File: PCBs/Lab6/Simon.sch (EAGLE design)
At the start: 17 parts

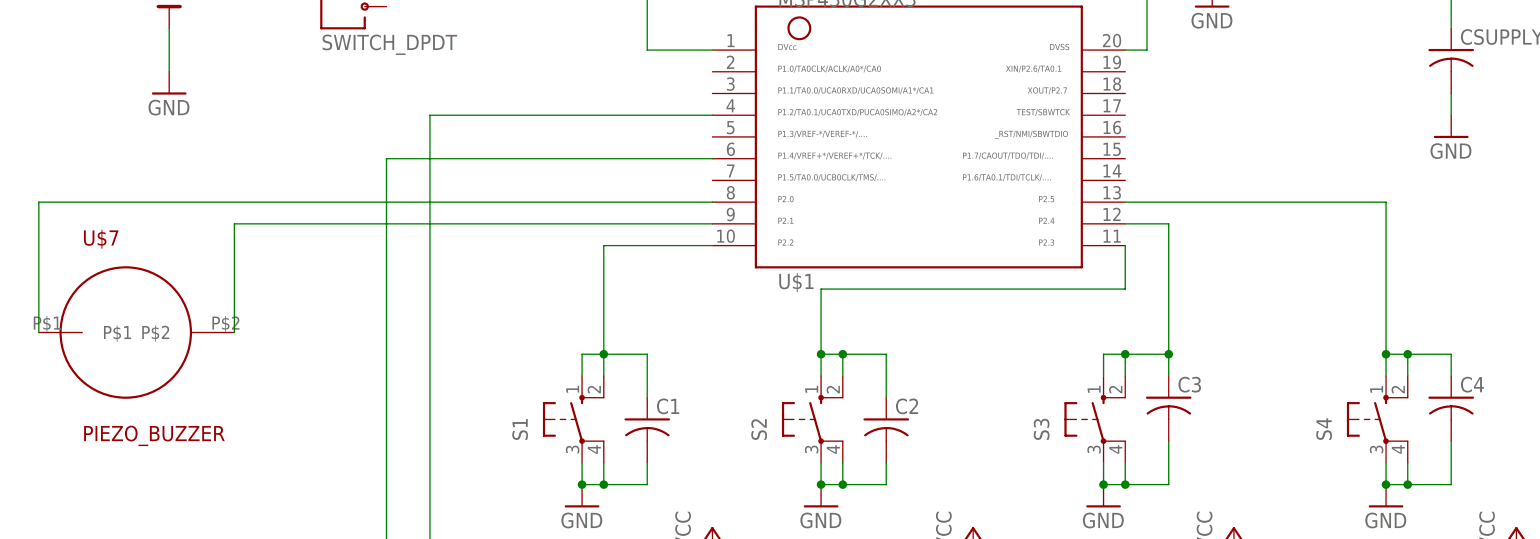
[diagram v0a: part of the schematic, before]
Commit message: Fixed buzzer connections
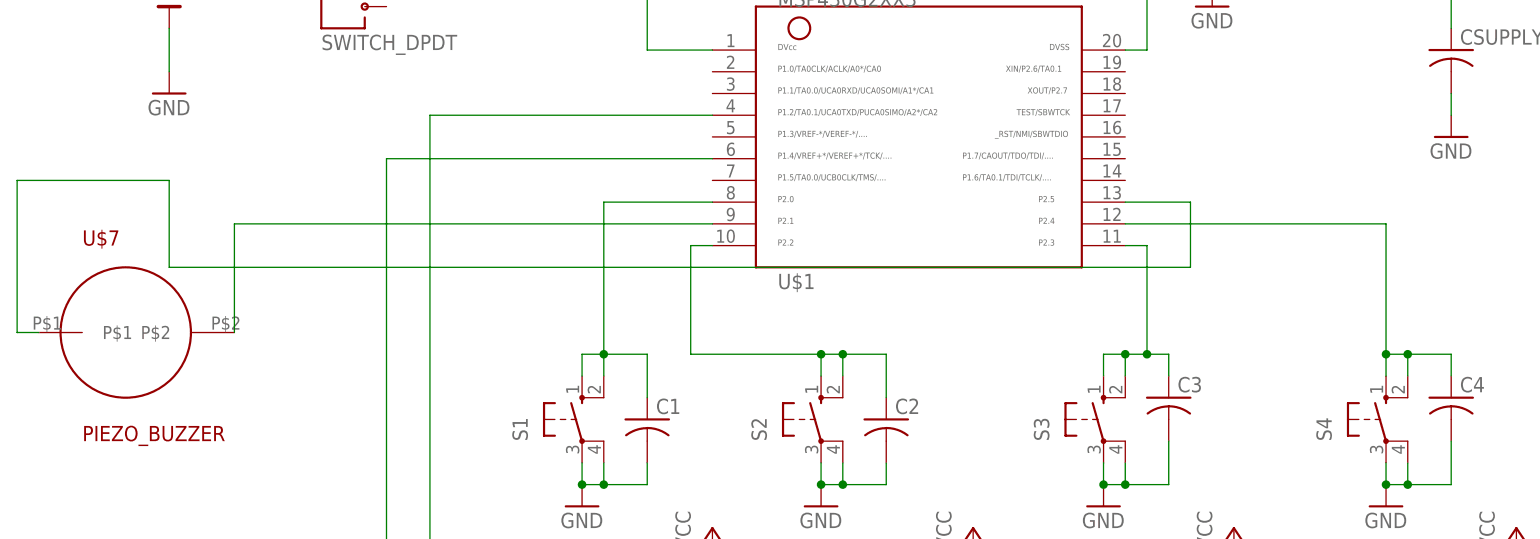
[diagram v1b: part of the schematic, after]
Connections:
- net N$11: now also U$1.13; no longer U$1.8
- net N$13: now also U$1.8; no longer U$1.10
- net N$14: now also U$1.10; no longer U$1.11
- net N$15: now also U$1.11; no longer U$1.12
- net N$16: now also U$1.12; no longer U$1.13
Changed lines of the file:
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@@
 <setting verticaltext="up"/>
 </settings>
-<grid distance="0.1" unitdist="inch" unit="inch" style="lines" multiple="1" display="yes" altdistance="0.01" altunitdist="inch" altunit="inch"/>
+<grid distance="0.1" unitdist="inch" unit="inch" style="lines" multiple="1" display="no" altdistance="0.01" altunitdist="inch" altunit="inch"/>
 <layers>
 <layer number="1" name="Top" color="4" fill="1" visible="no" active="no"/>
@@
 <wire x1="2.54" y1="-22.86" x2="2.54" y2="-27.94" width="0.1524" layer="91"/>
 <junction x="-2.54" y="-22.86"/>
-<pinref part="U$1" gate="G$1" pin="10"/>
-<wire x1="10.16" y1="-10.16" x2="-2.54" y2="-10.16" width="0.1524" layer="91"/>
-<wire x1="-2.54" y1="-10.16" x2="-2.54" y2="-22.86" width="0.1524" layer="91"/>
+<wire x1="-2.54" y1="-5.08" x2="-2.54" y2="-22.86" width="0.1524" layer="91"/>
+<pinref part="U$1" gate="G$1" pin="8"/>
+<wire x1="-2.54" y1="-5.08" x2="10.16" y2="-5.08" width="0.1524" layer="91"/>
 </segment>
 </net>
@@
 <wire x1="30.48" y1="-22.86" x2="30.48" y2="-27.94" width="0.1524" layer="91"/>
 <junction x="25.4" y="-22.86"/>
-<pinref part="U$1" gate="G$1" pin="11"/>
-<wire x1="58.42" y1="-10.16" x2="58.42" y2="-15.24" width="0.1524" layer="91"/>
-<wire x1="58.42" y1="-15.24" x2="22.86" y2="-15.24" width="0.1524" layer="91"/>
-<wire x1="22.86" y1="-15.24" x2="22.86" y2="-22.86" width="0.1524" layer="91"/>
+<pinref part="U$1" gate="G$1" pin="10"/>
+<wire x1="10.16" y1="-10.16" x2="7.62" y2="-10.16" width="0.1524" layer="91"/>
+<wire x1="7.62" y1="-10.16" x2="7.62" y2="-22.86" width="0.1524" layer="91"/>
+<wire x1="7.62" y1="-22.86" x2="22.86" y2="-22.86" width="0.1524" layer="91"/>
 </segment>
 </net>
@@
 <pinref part="C3" gate="G$1" pin="1"/>
 <wire x1="63.5" y1="-25.4" x2="63.5" y2="-22.86" width="0.1524" layer="91"/>
-<wire x1="63.5" y1="-22.86" x2="58.42" y2="-22.86" width="0.1524" layer="91"/>
+<wire x1="63.5" y1="-22.86" x2="60.96" y2="-22.86" width="0.1524" layer="91"/>
 <junction x="58.42" y="-22.86"/>
-<pinref part="U$1" gate="G$1" pin="12"/>
-<wire x1="58.42" y1="-7.62" x2="63.5" y2="-7.62" width="0.1524" layer="91"/>
-<wire x1="63.5" y1="-7.62" x2="63.5" y2="-22.86" width="0.1524" layer="91"/>
-<junction x="63.5" y="-22.86"/>
+<pinref part="U$1" gate="G$1" pin="11"/>
+<wire x1="60.96" y1="-22.86" x2="58.42" y2="-22.86" width="0.1524" layer="91"/>
+<wire x1="58.42" y1="-10.16" x2="60.96" y2="-10.16" width="0.1524" layer="91"/>
+<wire x1="60.96" y1="-10.16" x2="60.96" y2="-22.86" width="0.1524" layer="91"/>
+<junction x="60.96" y="-22.86"/>
 </segment>
 </net>
@@
 <segment>
 <pinref part="S4" gate="1" pin="S"/>
-<wire x1="88.9" y1="-5.08" x2="88.9" y2="-22.86" width="0.1524" layer="91"/>
 <pinref part="S4" gate="1" pin="S1"/>
+<wire x1="88.9" y1="-7.62" x2="88.9" y2="-22.86" width="0.1524" layer="91"/>
 <wire x1="88.9" y1="-22.86" x2="88.9" y2="-25.4" width="0.1524" layer="91"/>
 <wire x1="91.44" y1="-25.4" x2="91.44" y2="-22.86" width="0.1524" layer="91"/>
@@
 <wire x1="96.52" y1="-22.86" x2="96.52" y2="-25.4" width="0.1524" layer="91"/>
 <junction x="91.44" y="-22.86"/>
-<pinref part="U$1" gate="G$1" pin="13"/>
-<wire x1="58.42" y1="-5.08" x2="88.9" y2="-5.08" width="0.1524" layer="91"/>
+<pinref part="U$1" gate="G$1" pin="12"/>
+<wire x1="58.42" y1="-7.62" x2="88.9" y2="-7.62" width="0.1524" layer="91"/>
 </segment>
 </net>
@@
 <net name="N$11" class="0">
 <segment>
-<pinref part="U$1" gate="G$1" pin="8"/>
+<pinref part="U$1" gate="G$1" pin="13"/>
+<wire x1="58.42" y1="-5.08" x2="66.04" y2="-5.08" width="0.1524" layer="91"/>
+<wire x1="66.04" y1="-5.08" x2="66.04" y2="-12.7" width="0.1524" layer="91"/>
+<wire x1="66.04" y1="-12.7" x2="-53.34" y2="-12.7" width="0.1524" layer="91"/>
+<wire x1="-53.34" y1="-12.7" x2="-53.34" y2="-2.54" width="0.1524" layer="91"/>
+<wire x1="-53.34" y1="-2.54" x2="-71.12" y2="-2.54" width="0.1524" layer="91"/>
+<wire x1="-71.12" y1="-2.54" x2="-71.12" y2="-20.32" width="0.1524" layer="91"/>
 <pinref part="U$7" gate="G$1" pin="P$1"/>
-<wire x1="10.16" y1="-5.08" x2="-68.58" y2="-5.08" width="0.1524" layer="91"/>
-<wire x1="-68.58" y1="-5.08" x2="-68.58" y2="-20.32" width="0.1524" layer="91"/>
-</segment>
-</net>
+<wire x1="-71.12" y1="-20.32" x2="-68.58" y2="-20.32" width="0.1524" layer="91"/>
+</segment>
+</net>

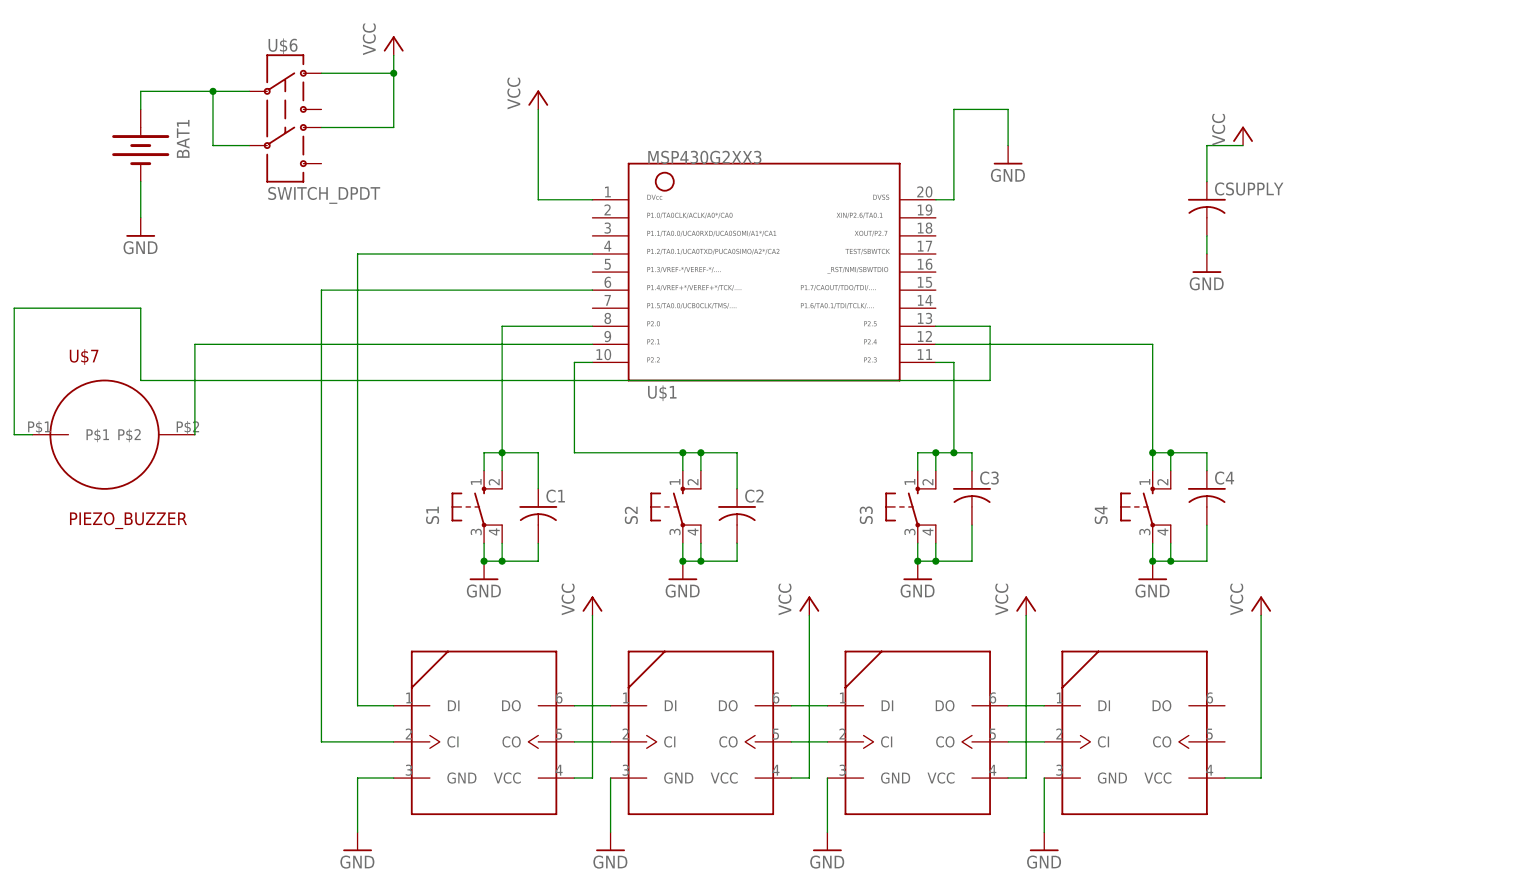
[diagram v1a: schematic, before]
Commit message: Switched to Xin Huang's schematic
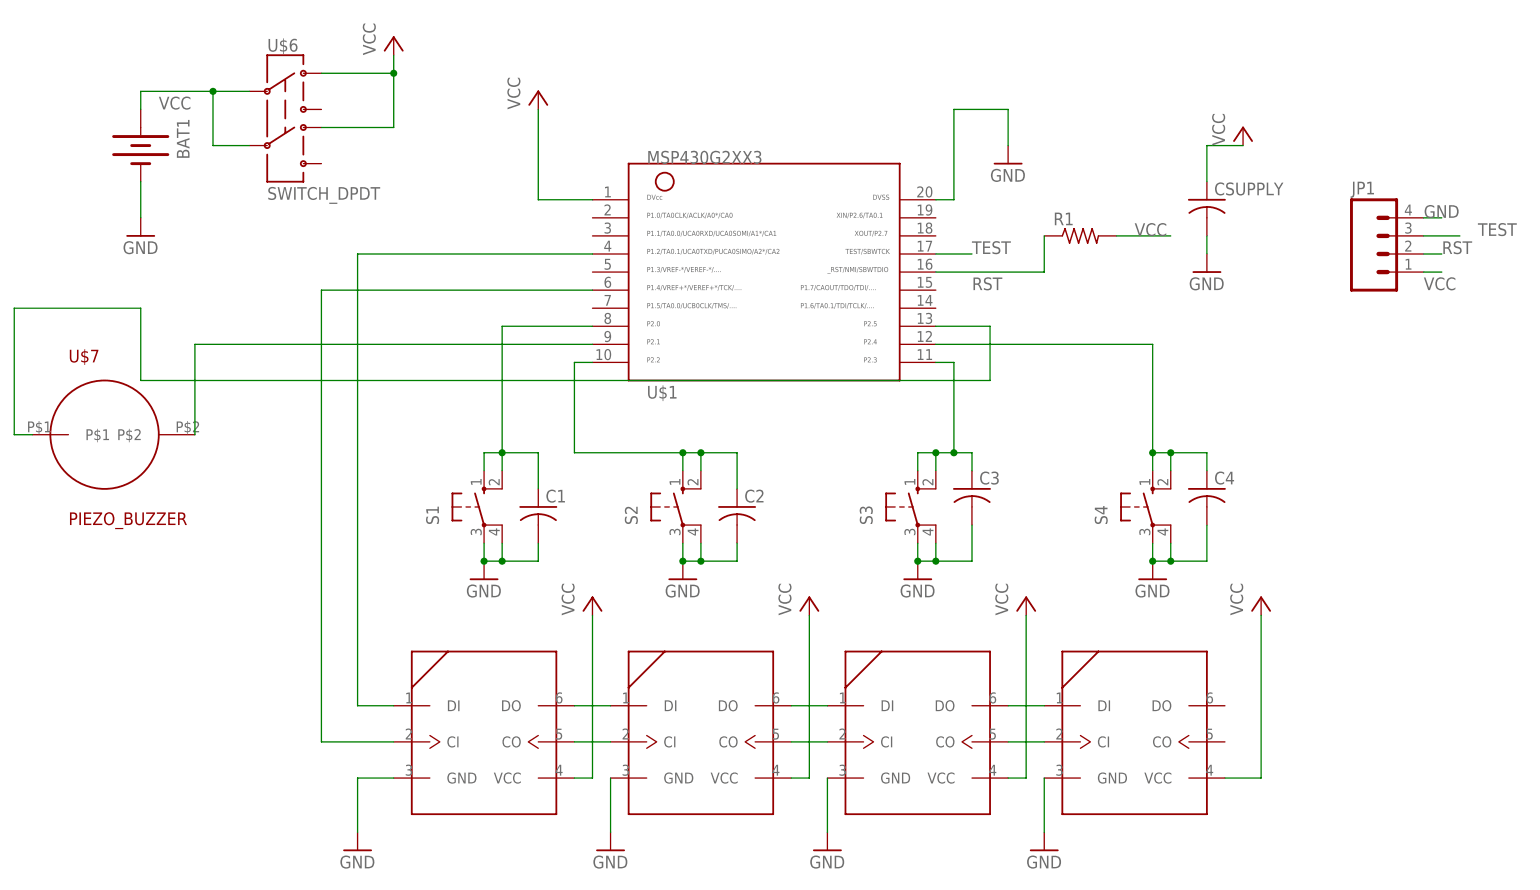
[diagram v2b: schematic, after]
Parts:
- added JP1: (no value), SparkFun:M04LOCK
- added R1: (no value), resistor:R-US_R1206
- renumbered U$2 to LED1, U$3 to LED2, U$4 to LED3, U$5 to LED4
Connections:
- removed net N$9: BAT1.+, U$6.2, U$6.5
- new net RST: JP1.2, R1.1, U$1.16
- new net TEST: JP1.3, U$1.17
- net GND: now also JP1.4
- net VCC: now also BAT1.+, JP1.1, R1.2, U$6.2, U$6.5

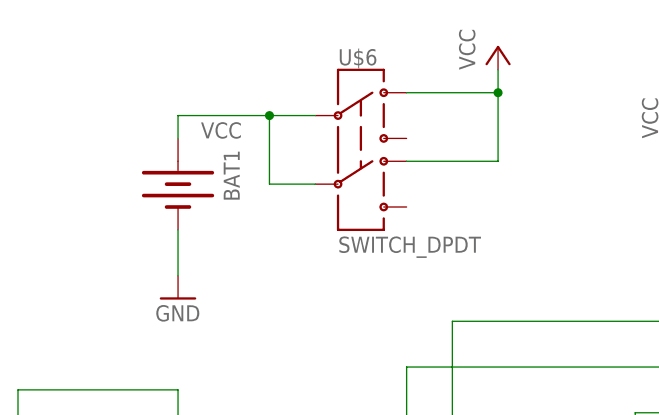
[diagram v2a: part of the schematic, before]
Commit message: Fixed VCC bug
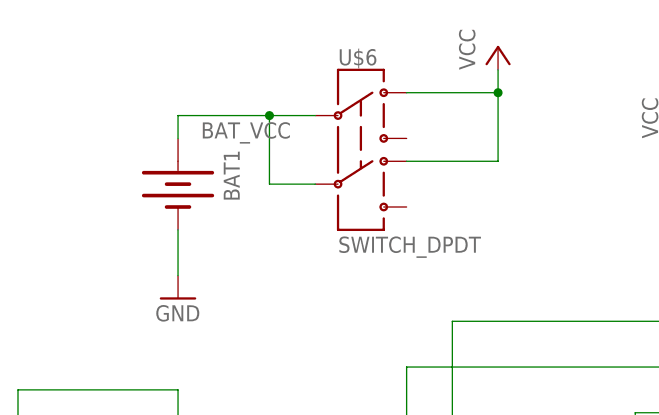
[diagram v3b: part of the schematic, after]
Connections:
- new net BAT_VCC: BAT1.+, U$6.2, U$6.5
- net VCC: no longer BAT1.+, U$6.2, U$6.5
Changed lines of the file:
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@@
 <label x="86.36" y="7.62" size="1.778" layer="95"/>
-</segment>
-<segment>
-<pinref part="U$6" gate="G$1" pin="2"/>
-<wire x1="-38.1" y1="27.94" x2="-43.18" y2="27.94" width="0.1524" layer="91"/>
-<pinref part="BAT1" gate="G$1" pin="+"/>
-<wire x1="-43.18" y1="27.94" x2="-53.34" y2="27.94" width="0.1524" layer="91"/>
-<wire x1="-53.34" y1="27.94" x2="-53.34" y2="25.4" width="0.1524" layer="91"/>
-<wire x1="-43.18" y1="27.94" x2="-43.18" y2="20.32" width="0.1524" layer="91"/>
-<junction x="-43.18" y="27.94"/>
-<pinref part="U$6" gate="G$1" pin="5"/>
-<wire x1="-38.1" y1="20.32" x2="-43.18" y2="20.32" width="0.1524" layer="91"/>
-<label x="-50.8" y="25.4" size="1.778" layer="95"/>
 </segment>
 </net>
@@
 </segment>
 </net>
+<net name="BAT_VCC" class="0">
+<segment>
+<pinref part="U$6" gate="G$1" pin="2"/>
+<wire x1="-38.1" y1="27.94" x2="-43.18" y2="27.94" width="0.1524" layer="91"/>
+<pinref part="BAT1" gate="G$1" pin="+"/>
+<wire x1="-43.18" y1="27.94" x2="-53.34" y2="27.94" width="0.1524" layer="91"/>
+<wire x1="-53.34" y1="27.94" x2="-53.34" y2="25.4" width="0.1524" layer="91"/>
+<wire x1="-43.18" y1="27.94" x2="-43.18" y2="20.32" width="0.1524" layer="91"/>
+<junction x="-43.18" y="27.94"/>
+<pinref part="U$6" gate="G$1" pin="5"/>
+<wire x1="-38.1" y1="20.32" x2="-43.18" y2="20.32" width="0.1524" layer="91"/>
+<label x="-50.8" y="25.4" size="1.778" layer="95"/>
+</segment>
+</net>
